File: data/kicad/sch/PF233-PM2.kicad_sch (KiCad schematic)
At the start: 17 parts, among them J1 MT60-M leads: BAT+ BAT- ILK, J3 Power switch pair (top housin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, Q1 P-MOSFET -40V

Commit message: Step 5: datasheets and fabricator sheets (vendor-derived floor, verified parts, PB1R 9-can bank, Gerber edge read-back)
- Fab floor from AdvancedPCB / TTM pages (docs/design/FAB_RULES_VERIFIED.md, U-FAB-RULES closed): clearance 0.16,
  component-PTH ring 0.18 / hole 0.46, drill-copper 0.26, drill-drill 0.41, every rule (severity error).
  CB1D JA/JB and HB2 TO-92 pads 1.02 mm; route_fix merges close same-net vias (CB1D, LB1).
- Parts from manufacturer PDFs (docs/design/DATASHEET_LOG.md): PB1R bulk 9 x Panasonic EEHZC1H101P
  (the 150 uF / 50 V polymer-Ta was not found; bank stays 900 uF, on-time table unchanged), PB1R re-placed
  with the Kelvin/comparator cluster pinned (pulse path 4.9 mohm, spike 7.5 V, ground ref 15.5 mV unchanged);
  SMCJ30A (SMCJ33A clamps 53.3 V > 50 V parts), Si4401FDY, BZT52C15, Bourns SF-1206S500-2 (new 1206 land),
  DRV5023BIQLPG, CRCW2512 500 V, OPA2365/OPA2211/LM393/CD74HC4051 checked. ES3J 600 V kept as a WATCH.
- U-DS-PARTS split into groups; open: TXDRIVE, OKI, PACK, BAV199, HVTERM. U-COLD-BOOTSTRAP closed.
- Controls retargeted to fixture folders (12/12). Netlist date fixed (data changed daily).
- Gerber planes from gerber_out.py ran into the notch and to 0.1 mm of the edge since r1 (found by the
  independent review): fixed, and gerber_edge_check.py reads every copper layer back.
- New Gerber sets CB1D_B3, LB1_v5, PB1R_v2; old sets marked SUPERSEDED.
- Findings for the owner: aluminium cans ~0.5 x a 1 g nugget (OPEN_ITEMS 34), OPA2365 capacitive load (30),
  OPA2211 input range on 5 V (31), Hall magnet spread (32).
- Strict regress 55 PASS / 0 FAIL / 0 SKIP; sign-off 44 PASS / 0 FAIL / 0 SKIP / 19 UNVERIFIED.

Co-Authored-By: Claude Opus 5.5 <noreply@anthropic.com>
Claude-Session: https://claude.ai/code/session_015VKhZtgEAWnezB2NDY75VV
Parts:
- CB1: value 470u 50V -> 100u 50V hybrid
- DTVS: value SMCJ33A -> SMCJ30A
- F1: footprint Fuse:Fuse_1812_4532Metric -> Fuse:Fuse_1206_3216Metric
- Q1: value P-MOSFET -40V -> Si4401FDY -40V
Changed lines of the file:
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@@
   (symbol (lib_id "PF233_auto:CB1") (at 30.48 40.64 0) (unit 1) (exclude_from_sim no) (in_bom yes) (on_board yes) (dnp no)
     (property "Reference" "CB1" (at 30.48 38.10 0) (effects (font (size 1.27 1.27))))
-    (property "Value" "470u 50V" (at 30.48 44.45 0) (effects (font (size 1.0 1.0))))
+    (property "Value" "100u 50V hybrid" (at 30.48 44.45 0) (effects (font (size 1.0 1.0))))
     (property "Footprint" "Capacitor_SMD:CP_Elec_10x10" (at 30.48 40.64 0) (effects (font (size 1.27 1.27)) hide))
     (pin "1")
@@
   (symbol (lib_id "PF233_auto:DTVS") (at 30.48 71.12 0) (unit 1) (exclude_from_sim no) (in_bom yes) (on_board yes) (dnp no)
     (property "Reference" "DTVS" (at 30.48 68.58 0) (effects (font (size 1.27 1.27))))
-    (property "Value" "SMCJ33A" (at 30.48 74.93 0) (effects (font (size 1.0 1.0))))
+    (property "Value" "SMCJ30A" (at 30.48 74.93 0) (effects (font (size 1.0 1.0))))
     (property "Footprint" "Diode_SMD:D_SMC" (at 30.48 71.12 0) (effects (font (size 1.27 1.27)) hide))
     (pin "1")
@@
     (property "Reference" "F1" (at 30.48 88.90 0) (effects (font (size 1.27 1.27))))
     (property "Value" "5A slow 32V" (at 30.48 95.25 0) (effects (font (size 1.0 1.0))))
-    (property "Footprint" "Fuse:Fuse_1812_4532Metric" (at 30.48 91.44 0) (effects (font (size 1.27 1.27)) hide))
+    (property "Footprint" "Fuse:Fuse_1206_3216Metric" (at 30.48 91.44 0) (effects (font (size 1.27 1.27)) hide))
     (pin "1")
     (pin "2")
@@
   (symbol (lib_id "PF233_auto:Q1") (at 30.48 147.32 0) (unit 1) (exclude_from_sim no) (in_bom yes) (on_board yes) (dnp no)
     (property "Reference" "Q1" (at 30.48 144.78 0) (effects (font (size 1.27 1.27))))
-    (property "Value" "P-MOSFET -40V" (at 30.48 158.75 0) (effects (font (size 1.0 1.0))))
+    (property "Value" "Si4401FDY -40V" (at 30.48 158.75 0) (effects (font (size 1.0 1.0))))
     (property "Footprint" "Package_SO:SOIC-8_3.9x4.9mm_P1.27mm" (at 30.48 147.32 0) (effects (font (size 1.27 1.27)) hide))
     (pin "1")

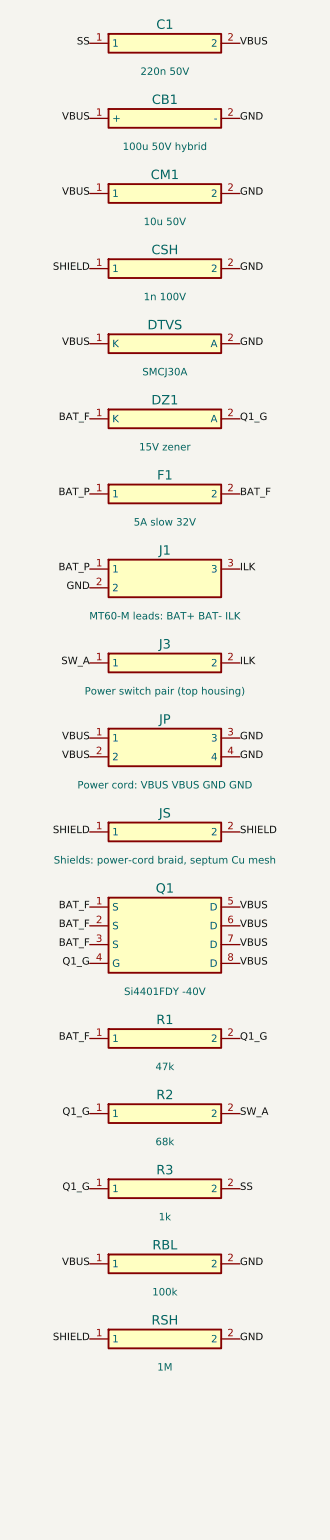
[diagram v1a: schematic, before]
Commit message: WIP (NOT signed off): data published by the first close-out sign-off run, which had 5 FAIL (CB1D-C2 / AU1 fine-pitch clearance); superseded by the rerun in progress
Co-Authored-By: Claude Opus 5.5 <noreply@anthropic.com>
Claude-Session: https://claude.ai/code/session_01FX4DWSYYjMCFGGA6gmha65
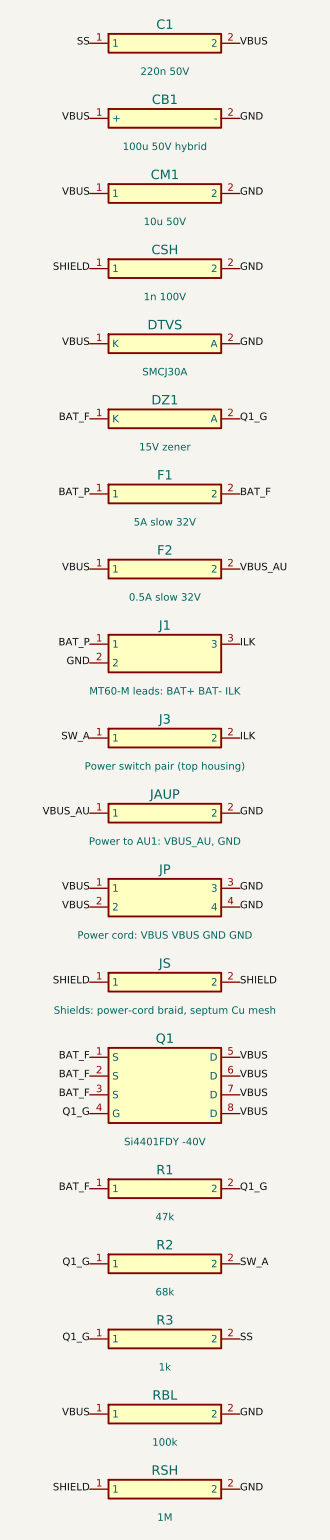
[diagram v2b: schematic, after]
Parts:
- added F2: 0.5A slow 32V, Fuse:Fuse_1206_3216Metric, symbol PF233_auto:F2
- added JAUP: Power to AU1: VBUS_AU, GND, Connector:SolderPad_2x_P5.08mm, symbol PF233_auto:JAUP
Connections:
- net GND: now also JAUP.2
- net VBUS: now also F2.1
- new net VBUS_AU: F2.2, JAUP.1
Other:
- moved on the sheet: J1, J3, JP, JS, Q1, R1, R2, R3, RBL, RSH
